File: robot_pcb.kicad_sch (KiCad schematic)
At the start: 55 parts, among them J1 Raspberry_Pi_2_3, J10 Servo_TrayRelease, J11 BATT BYPASS, J12 12V BYPASS, J13 MAX14870, J14 MAX14870, J15 MAX14870, J16 MAX14870, J17 Conn_01x04, J18 USB_C_Receptacle_PowerOnly_6P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

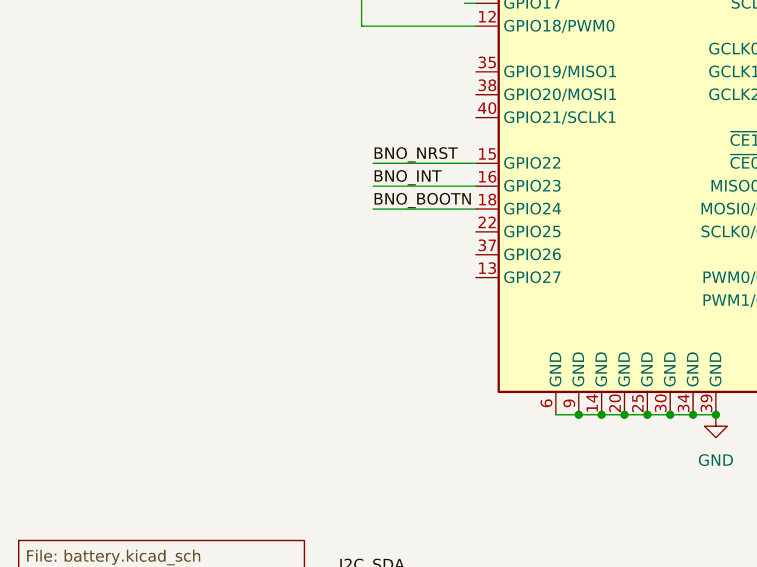
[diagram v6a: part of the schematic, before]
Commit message: conductive test claw
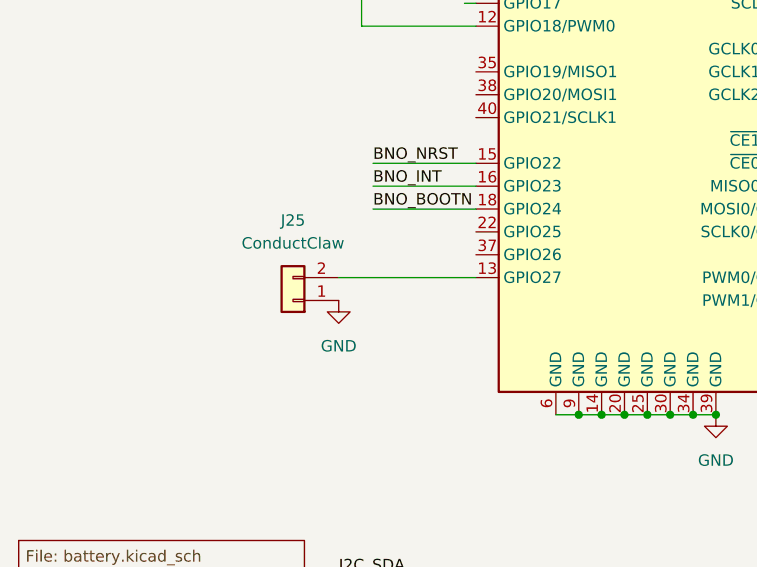
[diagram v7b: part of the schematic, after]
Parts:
- added J25: ConductClaw, Connector_JST:JST_PH_B2B-PH-K_1x02_P2.00mm_Vertical, symbol Connector_Generic:Conn_01x02
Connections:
- net GND: now also J25.1 (Pin_1)
- net at J1.13 (GPIO27): now also J25.2 (Pin_2)
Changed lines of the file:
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@@
 	(wire
 		(pts
+			(xy 49.53 85.09) (xy 64.77 85.09)
+		)
+		(stroke
+			(width 0)
+			(type default)
+		)
+	)
+	(wire
+		(pts
 			(xy 248.92 256.54) (xy 247.65 256.54)
 		)
@@
 	)
 	(symbol
+		(lib_id "Connector_Generic:Conn_01x02")
+		(at 44.45 87.63 180)
+		(unit 1)
+		(exclude_from_sim no)
+		(in_bom yes)
+		(on_board yes)
+		(dnp no)
+		(fields_autoplaced yes)
+		(property "Reference" "J25"
+			(at 44.45 78.74 0)
+			(effects
+				(font
+					(size 1.27 1.27)
+				)
+			)
+		)
+		(property "Value" "ConductClaw"
+			(at 44.45 81.28 0)
+			(effects
+				(font
+					(size 1.27 1.27)
+				)
+			)
+		)
+		(property "Footprint" "Connector_JST:JST_PH_B2B-PH-K_1x02_P2.00mm_Vertical"
+			(at 44.45 87.63 0)
+			(effects
+				(font
+					(size 1.27 1.27)
+				)
+				(hide yes)
+			)
+		)
+		(property "Datasheet" "~"
+			(at 44.45 87.63 0)
+			(effects
+				(font
+					(size 1.27 1.27)
+				)
+				(hide yes)
+			)
+		)
+		(property "Description" "Generic connector, single row, 01x02, script generated (kicad-library-utils/schlib/autogen/connector/)"
+			(at 44.45 87.63 0)
+			(effects
+				(font
+					(size 1.27 1.27)
+				)
+				(hide yes)
+			)
+		)
+		(pin "1"
+		)
+		(pin "2"
+		)
+		(instances
+			(project ""
+				(path "/2f56b371-1597-47e1-a48d-b7f69d342f77"
+					(reference "J25")
+					(unit 1)
+				)
+			)
+		)
+	)
+	(symbol
 		(lib_id "power:+3.3V")
 		(at 224.79 63.5 90)
@@
 					(unit 1)
 				)
+			)
+		)
+	)
+	(symbol
+		(lib_id "power:GND")
+		(at 49.53 87.63 0)
+		(unit 1)
+		(exclude_from_sim no)
+		(in_bom yes)
+		(on_board yes)
+		(dnp no)
+		(fields_autoplaced yes)
+		(property "Reference" "#PWR084"
+			(at 49.53 93.98 0)
+			(effects
+				(font
+					(size 1.27 1.27)
+				)
+				(hide yes)
+			)
+		)
+		(property "Value" "GND"
+			(at 49.53 92.71 0)
+			(effects
+				(font
+					(size 1.27 1.27)
+				)
+			)
+		)
+		(property "Footprint" ""
+			(at 49.53 87.63 0)
+			(effects
+				(font
+					(size 1.27 1.27)
+				)
+				(hide yes)
+			)
+		)
+		(property "Datasheet" ""
+			(at 49.53 87.63 0)
+			(effects
+				(font
+					(size 1.27 1.27)
+				)
+				(hide yes)
+			)
+		)
+		(property "Description" "Power symbol creates a global label with name \"GND\" , ground"
+			(at 49.53 87.63 0)
+			(effects
+				(font
+					(size 1.27 1.27)
+				)
+				(hide yes)
+			)
+		)
+		(pin "1"
+		)
+		(instances
+			(project ""
+				(path "/2f56b371-1597-47e1-a48d-b7f69d342f77"
+					(reference "#PWR084")
+					(unit 1)
+				)

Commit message: Update robot_pcb.kicad_sch
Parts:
- added J26: Conn_01x05, symbol Connector_Generic:Conn_01x05
- added U10, U11: DMG2305UX-7, Package_TO_SOT_SMD:TSOT-23, symbol Transistor_FET:DMG2305UX-7
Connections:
- net +3.3V: now also J26.2 (Pin_2)
- net +5V: now also U10.2 (S), U11.2 (S); no longer J10.2 (Pin_2), J8.2 (Pin_2), J9.2 (Pin_2)
- net GND: now also J26.1 (Pin_1)
- net I2C_SCL: now also J26.4 (Pin_4)
- net I2C_SDA: now also J26.3 (Pin_3)
- net GPIO25: now reaches J1.22 (GPIO25)
- net GPIO25: now also J26.5 (Pin_5)
- net GPIO0: now reaches J1.27 (ID_SD/GPIO0)
- net GPIO0: now also U10.1 (G)
- net GPIO1: now reaches J1.28 (ID_SC/GPIO1)
- net GPIO1: now also U11.1 (G)
- new net: J10.2 (Pin_2), J8.2 (Pin_2), U11.3 (D)
- new net: J9.2 (Pin_2), U10.3 (D)
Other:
- moved on the sheet: J10, J22, J23, J7, J8, J9, U5
